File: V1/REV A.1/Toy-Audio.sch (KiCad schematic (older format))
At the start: 18 parts, among them J1 CONN_2, J2 CONN_01X04, J3 CONN_01X10, Q1 Si2302DS, U1 XC6206P332MR, U2 STM32F030F4P6, U3 W25Q32FVSIG

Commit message: Added Standby mode to software V1. Modified hardware to support Standby (add pull up/down resistors) todo hardware V3
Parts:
- removed SP1: 16Ohm, MvdL:JST-PH-2P-DUAL, symbol SPEAKER
- added R?: 1k5, MvdL:R0603, symbol RR
- added SP1: CONN_01X02, symbol CONN_01X02
- C4: value 10u -> 1u
- C8: value d.n.p -> 22n
- Q1: value Si2302DS -> DNP
- R3: value 0R -> DNP
- U3: value W25Q32FVSIG -> W25Q128FVSIG
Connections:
- net labels added: ~CS-FL
- net labels removed: nCS
- wire segments 84 -> 85
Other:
- note added: "10n"
- note added: "1k5"
- note added: "LPF with 4KHz cutoff to filter \nout the PWM base frequency"
- note added: "Modified circuit for audio output (connect audio amp to audio out)"
- note added: "PA0 = WKUP1"
- note added: "audio out"
- note added: "connect to ground"
- note added: "replace Q1 by a 1k resistor\nbetween G and D"
- note removed: "12k"
- note removed: "3V"
- note removed: "Do not place U1 when using 3V battery power\nbypass pin 2 and 3"
- note removed: "Optional HPF with 4KHz cutoff to filter \nout the PWM base frequency"
- note removed: "d.n.p. = do not place"
- moved on the sheet: C10, C8, R3

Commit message: Improved Wake-up pin stability WKUP1. modiefied schematic files. Software V1 is compatible with hardware V2
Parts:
- C8: value 22n -> 47n
- R?: value 1k5 -> d.n.p
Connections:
- net UART1_EN renamed ~Mute
- net USART1_CTS renamed WKUP1
- net ~CS-FL renamed ~CS0
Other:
- note added: "100k"
- note added: "10k"
- note added: "910R"
- note added: "replace Q1 by a 910 Ohm resistor\nbetween G and D"
- note removed: "10n"
- note removed: "1k5"
- note removed: "replace Q1 by a 1k resistor\nbetween G and D"
- moved on the sheet: J3
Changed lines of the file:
@@
 Text Notes 1250 3150 0    60   ~ 0
 STLink SWD Interface
-Text Label 6800 2450 0    60   ~ 0
+Text Label 7375 2475 0    60   ~ 0
 SCL1
-Text Label 6800 2350 0    60   ~ 0
+Text Label 7375 2375 0    60   ~ 0
 SDA1
 $Comp
@@
 $EndComp
 Text Label 5450 4300 0    60   ~ 0
-~CS-FL
+~CS0
 Text Notes 1250 4850 0    60   ~ 0
 Battery Power
@@
 	1    0    0    -1
 $EndComp
-Text Label 6800 2150 0    60   ~ 0
+Text Label 7375 2175 0    60   ~ 0
 USART1_TX
-Text Label 6800 2050 0    60   ~ 0
+Text Label 7375 2075 0    60   ~ 0
 USART1_RX
-Text Label 6800 1950 0    60   ~ 0
+Text Label 7375 1975 0    60   ~ 0
 USART1_CK
-Text Label 6800 1750 0    60   ~ 0
-UART1_EN
+Text Label 7375 1775 0    60   ~ 0
+~Mute
 $Comp
 L GND #PWR21
 U 1 1 55E01A86
-P 7500 2550
-F 0 "#PWR21" H 7500 2300 50  0001 C CNN
-F 1 "GND" H 7500 2400 50  0000 C CNN
-F 2 "" H 7500 2550 60  0000 C CNN
-F 3 "" H 7500 2550 60  0000 C CNN
-	1    7500 2550
+P 8075 2575
+F 0 "#PWR21" H 8075 2325 50  0001 C CNN
+F 1 "GND" H 8075 2425 50  0000 C CNN
+F 2 "" H 8075 2575 60  0000 C CNN
+F 3 "" H 8075 2575 60  0000 C CNN
+	1    8075 2575
 	1    0    0    -1
 $EndComp
@@
 L VDD #PWR20
 U 1 1 55E01CC1
-P 7400 1550
-F 0 "#PWR20" H 7400 1400 50  0001 C CNN
-F 1 "VDD" H 7400 1700 50  0000 C CNN
-F 2 "" H 7400 1550 60  0000 C CNN
-F 3 "" H 7400 1550 60  0000 C CNN
-	1    7400 1550
-	1    0    0    -1
-$EndComp
-Text Notes 7000 2950 0    60   ~ 0
+P 7975 1575
+F 0 "#PWR20" H 7975 1425 50  0001 C CNN
+F 1 "VDD" H 7975 1725 50  0000 C CNN
+F 2 "" H 7975 1575 60  0000 C CNN
+F 3 "" H 7975 1575 60  0000 C CNN
+	1    7975 1575
+	1    0    0    -1
+$EndComp
+Text Notes 7575 2975 0    60   ~ 0
 nRF24L01 interface\n+I2C
 $Comp
@@
 P 9200 3450
 F 0 "C8" H 9200 3550 40  0000 L CNN
-F 1 "22n" H 9206 3365 40  0000 L CNN
+F 1 "47n" H 9206 3365 40  0000 L CNN
 F 2 "MvdL:C0603" H 9238 3300 30  0001 C CNN
 F 3 "~" H 9200 3450 60  0000 C CNN
@@
 PWM
 Text Label 3300 1700 0    60   ~ 0
-~CS-FL
+~CS0
 Text Label 6050 2500 2    60   ~ 0
 SCK1
@@
 USART1_CK
 Text Label 3300 2100 0    60   ~ 0
-USART1_CTS
-Text Label 6800 1850 0    60   ~ 0
-USART1_CTS
+WKUP1
+Text Label 7375 1875 0    60   ~ 0
+WKUP1
 Text Label 3300 2200 0    60   ~ 0
 USART1_RTS
-Text Label 6800 2250 0    60   ~ 0
+Text Label 7375 2275 0    60   ~ 0
 USART1_RTS
 Text Label 6050 1600 2    60   ~ 0
@@
 SCL1
 Text Label 3300 1800 0    60   ~ 0
-UART1_EN
+~Mute
 $Comp
 L VCC #PWR2
@@
 L CONN_01X10 J3
 U 1 1 55EE328F
-P 7800 2000
-F 0 "J3" H 7800 2550 50  0000 C CNN
-F 1 "CONN_01X10" V 7900 2000 50  0000 C CNN
-F 2 "MvdL:HDR_5x2" H 7800 2000 60  0001 C CNN
-F 3 "" H 7800 2000 60  0000 C CNN
-	1    7800 2000
+P 8375 2025
+F 0 "J3" H 8375 2575 50  0000 C CNN
+F 1 "CONN_01X10" V 8475 2025 50  0000 C CNN
+F 2 "MvdL:HDR_5x2" H 8375 2025 60  0001 C CNN
+F 3 "" H 8375 2025 60  0000 C CNN
+	1    8375 2025
 	1    0    0    -1
 $EndComp
@@
 P 8950 3450
 F 0 "R?" V 9030 3450 50  0000 C CNN
-F 1 "1k5" V 8875 3450 50  0000 C CNN
+F 1 "d.n.p" V 8875 3450 50  0000 C CNN
 F 2 "MvdL:R0603" H 8950 3450 60  0001 C CNN
 F 3 "" H 8950 3450 60  0000 C CNN
@@
 	5050 4750 5050 4800
 Wire Wire Line
-	7500 2550 7500 1550
-Wire Wire Line
-	7500 1550 7600 1550
-Wire Wire Line
-	7600 1650 7400 1650
-Wire Wire Line
-	7400 1650 7400 1550
-Wire Wire Line
-	6800 1750 7600 1750
-Wire Wire Line
-	6800 1850 7600 1850
-Wire Wire Line
-	6800 1950 7600 1950
-Wire Wire Line
-	6800 2050 7600 2050
-Wire Wire Line
-	6800 2150 7600 2150
-Wire Wire Line
-	6800 2250 7600 2250
+	8075 2575 8075 1575
+Wire Wire Line
+	8075 1575 8175 1575
+Wire Wire Line
+	8175 1675 7975 1675
+Wire Wire Line
+	7975 1675 7975 1575
+Wire Wire Line
+	7375 1775 8175 1775
+Wire Wire Line
+	7375 1875 8175 1875
+Wire Wire Line
+	7375 1975 8175 1975
+Wire Wire Line
+	7375 2075 8175 2075
+Wire Wire Line
+	7375 2175 8175 2175
+Wire Wire Line
+	7375 2275 8175 2275
 Wire Wire Line
 	9200 4250 9200 4350
@@
 	6200 2000 5700 2000
 Wire Wire Line
-	6800 2350 7600 2350
-Wire Wire Line
-	7600 2450 6800 2450
+	7375 2375 8175 2375
+Wire Wire Line
+	8175 2475 7375 2475
 Wire Wire Line
 	2450 1800 2450 1850
@@
 	8950 3250 8950 3200
 Connection ~ 9200 3200
-Text Notes 7700 4450 0    60   ~ 0
-replace Q1 by a 1k resistor\nbetween G and D
+Text Notes 7525 4450 0    60   ~ 0
+replace Q1 by a 910 Ohm resistor\nbetween G and D
 Wire Notes Line
 	9050 2700 9400 3100
@@
 Wire Notes Line
 	9100 3950 9300 4200
-Text Notes 8850 3900 0    60   ~ 0
-1k5
+Text Notes 8800 3900 0    60   ~ 0
+910R
 Wire Notes Line
 	10400 3350 10800 3750
@@
 Text Notes 9550 3750 0    60   ~ 0
 audio out
-Wire Notes Line
-	9350 3950 9550 3950
-Wire Notes Line
-	9350 4000 9550 4000
-Wire Notes Line
-	9450 3950 9450 3850
-Wire Notes Line
-	9450 3850 9200 3850
-Wire Notes Line
-	9450 4000 9450 4250
-Wire Notes Line
-	9450 4250 9200 4250
-Text Notes 9550 4100 0    60   ~ 0
-10n
 Entry Bus Bus
 	4600 7250 4700 7350
@@
 Text Notes 7800 4750 0    60   ~ 0
 Modified circuit for audio output (connect audio amp to audio out)
+Wire Notes Line
+	7375 1875 7175 1875
+Wire Notes Line
+	7175 1875 7175 1925
+Wire Notes Line
+	7175 1925 7125 1950
+Wire Notes Line
+	7125 1950 7225 1975
+Wire Notes Line
+	7225 1975 7125 2000
+Wire Notes Line
+	7125 2000 7225 2025
+Wire Notes Line
+	7225 2025 7125 2050
+Wire Notes Line
+	7125 2050 7225 2075
+Wire Notes Line
+	7225 2075 7175 2100
+Wire Notes Line
+	7175 2100 7175 2550
+Wire Notes Line
+	7125 2550 7225 2550
+Wire Notes Line
+	7125 2550 7175 2600
+Wire Notes Line
+	7175 2600 7225 2550
+Wire Notes Line
+	7375 1775 6975 1775
+Wire Notes Line
+	6975 1775 6975 1900
+Wire Notes Line
+	6975 1900 6925 1925
+Wire Notes Line
+	6925 1925 7025 1950
+Wire Notes Line
+	7025 1950 6925 1975
+Wire Notes Line
+	6925 1975 7025 2000
+Wire Notes Line
+	7025 2000 6925 2025
+Wire Notes Line
+	6925 2025 7025 2050
+Wire Notes Line
+	7025 2050 6925 2075
+Wire Notes Line
+	6925 2075 6975 2100
+Wire Notes Line
+	6975 2100 6975 2550
+Wire Notes Line
+	6925 2550 7025 2550
+Wire Notes Line
+	6925 2550 6975 2600
+Wire Notes Line
+	6975 2600 7025 2550
+Text Notes 6700 1975 0    60   ~ 0
+100k
+Text Notes 7200 2175 0    60   ~ 0
+10k
 $EndSCHEMATC

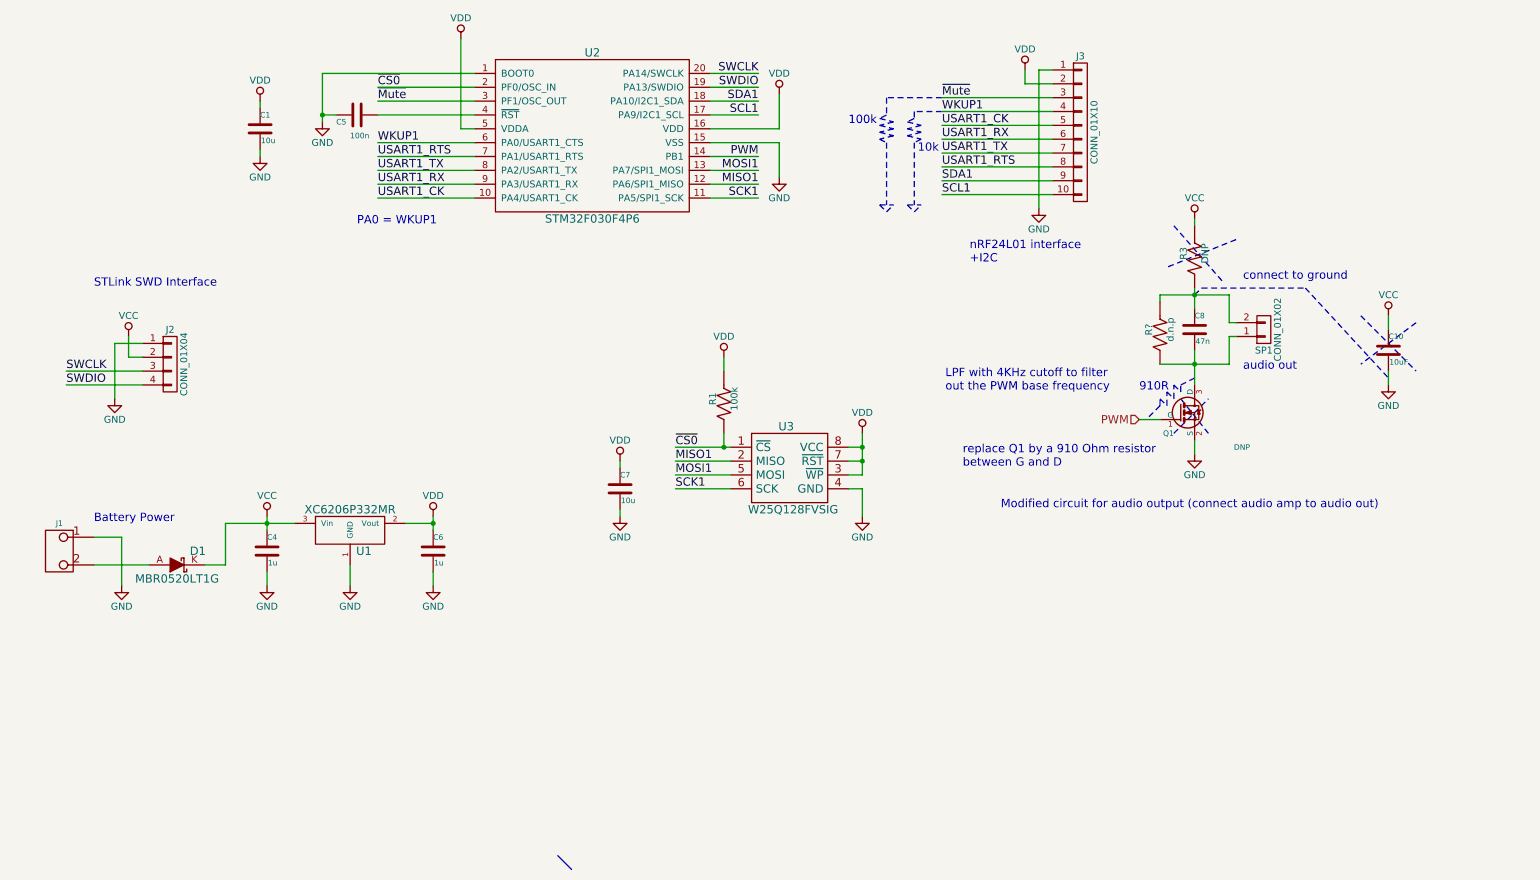
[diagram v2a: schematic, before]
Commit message: Modified/added documentation HW V1. changed SPI flash write function to wait for data transmision complete flag.
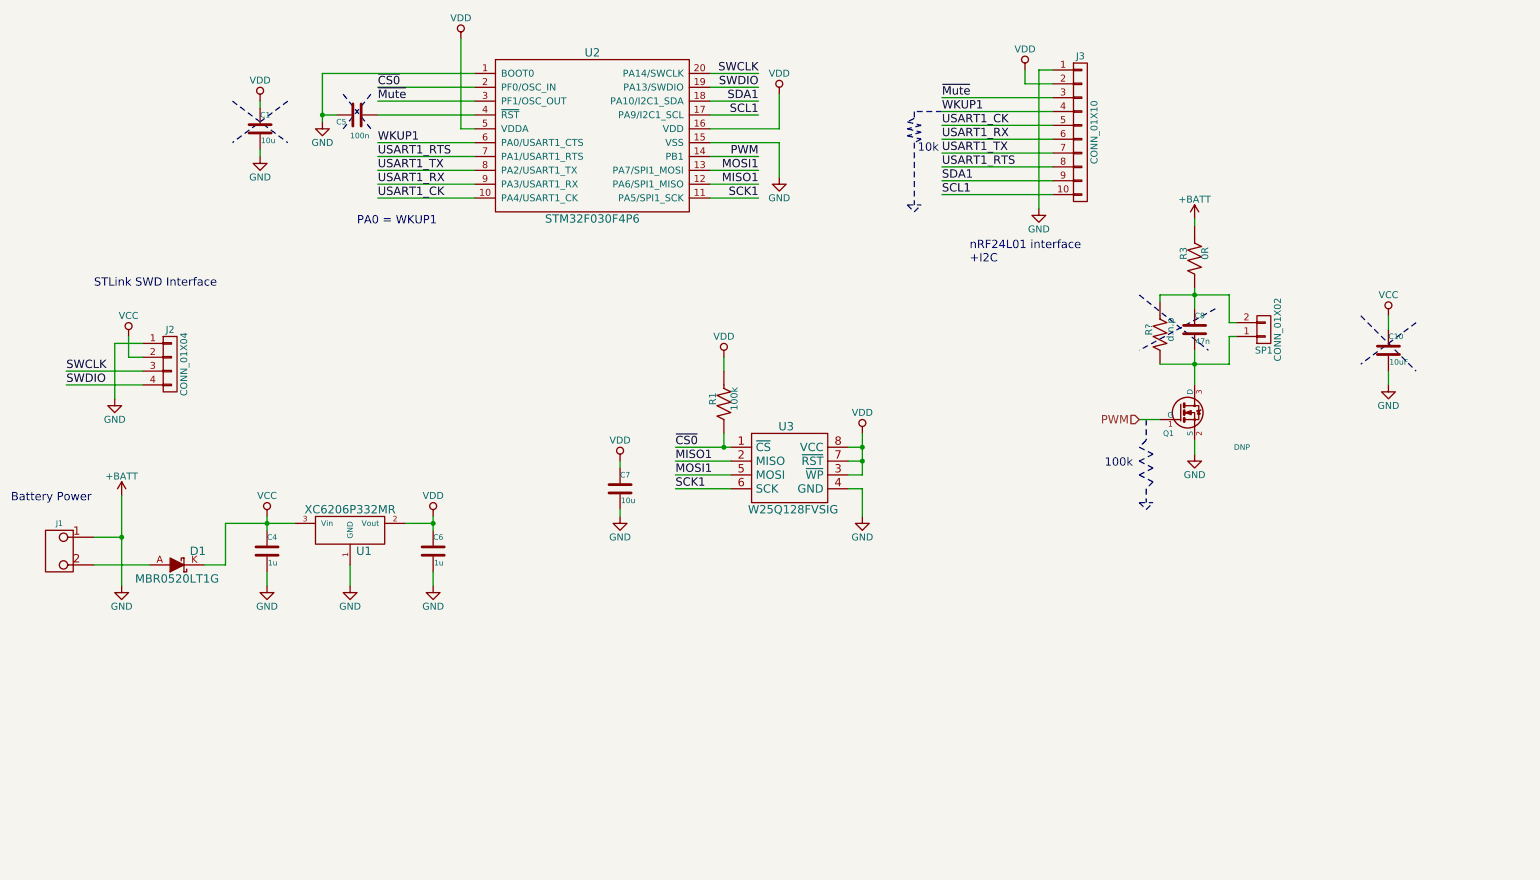
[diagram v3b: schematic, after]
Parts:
- R3: value DNP -> 0R
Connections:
- net VCC: no longer R3.2
- net GND renamed +BATT
- net +BATT: now also R3.2
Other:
- note removed: "910R"
- note removed: "LPF with 4KHz cutoff to filter \nout the PWM base frequency"
- note removed: "Modified circuit for audio output (connect audio amp to audio out)"
- note removed: "audio out"
- note removed: "connect to ground"
- note removed: "replace Q1 by a 910 Ohm resistor\nbetween G and D"
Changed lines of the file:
@@
 Sheet 1 1
 Title "Toy Audio V1"
-Date "5 aug 2015"
+Date "2016-02-07"
 Rev "A.1"
 Comp "Maurits van de Lande (maurits@vandelande.com)"
@@
 Text Label 5450 4300 0    60   ~ 0
 ~CS0
-Text Notes 1250 4850 0    60   ~ 0
+Text Notes 650  4700 0    60   ~ 0
 Battery Power
 Text Label 1050 3750 0    60   ~ 0
@@
 P 9200 2900
 F 0 "R3" V 9280 2900 50  0000 C CNN
-F 1 "DNP" V 9125 2900 50  0000 C CNN
+F 1 "0R" V 9125 2900 50  0000 C CNN
 F 2 "MvdL:R0603" H 9200 2900 60  0001 C CNN
 F 3 "" H 9200 2900 60  0000 C CNN
@@
 $EndComp
 $Comp
-L VCC #PWR22
-U 1 1 55EE2A6B
-P 9200 2650
-F 0 "#PWR22" H 9200 2500 50  0001 C CNN
-F 1 "VCC" H 9200 2800 50  0000 C CNN
-F 2 "" H 9200 2650 60  0000 C CNN
-F 3 "" H 9200 2650 60  0000 C CNN
-	1    9200 2650
-	1    0    0    -1
-$EndComp
-$Comp
 L CONN_01X10 J3
 U 1 1 55EE328F
@@
 	1    0    0    -1
 $EndComp
-Text Notes 7400 3900 0    60   ~ 0
-LPF with 4KHz cutoff to filter \nout the PWM base frequency
 $Comp
 L CONN_01X02 SP1
@@
 	2500 5300 2500 5200
 Wire Wire Line
-	1450 5300 1450 4950
+	1450 4650 1450 5300
 Wire Wire Line
 	1450 4950 1250 4950
@@
 	8950 3250 8950 3200
 Connection ~ 9200 3200
-Text Notes 7525 4450 0    60   ~ 0
-replace Q1 by a 910 Ohm resistor\nbetween G and D
-Wire Notes Line
-	9050 2700 9400 3100
-Wire Notes Line
-	9500 2800 9000 3000
-Wire Notes Line
-	8950 4000 8950 3950
-Wire Notes Line
-	8950 3950 9000 4000
-Wire Notes Line
-	9000 4000 9000 3900
-Wire Notes Line
-	9000 3900 9050 3950
-Wire Notes Line
-	9050 3950 9050 3850
-Wire Notes Line
-	9050 3850 9100 3900
-Wire Notes Line
-	9100 3900 9100 3850
-Wire Notes Line
-	9100 3850 9200 3800
-Wire Notes Line
-	8950 4000 8850 4100
-Wire Notes Line
-	9050 4200 9300 3950
-Wire Notes Line
-	9100 3950 9300 4200
-Text Notes 8800 3900 0    60   ~ 0
-910R
 Wire Notes Line
 	10400 3350 10800 3750
 Wire Notes Line
 	10800 3400 10400 3700
-Wire Notes Line
-	10000 3150 10600 3800
-Wire Wire Line
-	8950 3200 9450 3200
-Wire Notes Line
-	9200 3200 9250 3150
-Wire Notes Line
-	9250 3150 10000 3150
-Text Notes 9550 3100 0    60   ~ 0
-connect to ground
-Text Notes 9550 3750 0    60   ~ 0
-audio out
-Entry Bus Bus
-	4600 7250 4700 7350
 Text Notes 3150 2700 0    60   ~ 0
 PA0 = WKUP1
-Text Notes 7800 4750 0    60   ~ 0
-Modified circuit for audio output (connect audio amp to audio out)
 Wire Notes Line
 	7375 1875 7175 1875
@@
 Wire Notes Line
 	7175 2600 7225 2550
-Wire Notes Line
-	7375 1775 6975 1775
-Wire Notes Line
-	6975 1775 6975 1900
-Wire Notes Line
-	6975 1900 6925 1925
-Wire Notes Line
-	6925 1925 7025 1950
-Wire Notes Line
-	7025 1950 6925 1975
-Wire Notes Line
-	6925 1975 7025 2000
-Wire Notes Line
-	7025 2000 6925 2025
-Wire Notes Line
-	6925 2025 7025 2050
-Wire Notes Line
-	7025 2050 6925 2075
-Wire Notes Line
-	6925 2075 6975 2100
-Wire Notes Line
-	6975 2100 6975 2550
-Wire Notes Line
-	6925 2550 7025 2550
-Wire Notes Line
-	6925 2550 6975 2600
-Wire Notes Line
-	6975 2600 7025 2550
-Text Notes 6700 1975 0    60   ~ 0
-100k
 Text Notes 7200 2175 0    60   ~ 0
 10k
+Wire Wire Line
+	8950 3200 9450 3200
+Wire Notes Line
+	8800 3200 9300 3600
+Wire Notes Line
+	9350 3300 8800 3600
+Wire Notes Line
+	8850 4100 8850 4250
+Wire Notes Line
+	8850 4250 8800 4300
+Wire Notes Line
+	8800 4300 8900 4350
+Wire Notes Line
+	8900 4350 8800 4400
+Wire Notes Line
+	8800 4400 8900 4450
+Wire Notes Line
+	8900 4450 8800 4500
+Wire Notes Line
+	8800 4500 8900 4550
+Wire Notes Line
+	8900 4550 8850 4600
+Wire Notes Line
+	8850 4600 8850 4700
+Wire Notes Line
+	8800 4700 8900 4700
+Wire Notes Line
+	8800 4700 8850 4750
+Wire Notes Line
+	8850 4750 8900 4700
+Text Notes 8550 4450 0    60   ~ 0
+100k
+$Comp
+L +BATT #PWR?
+U 1 1 56B7E010
+P 9200 2650
+F 0 "#PWR?" H 9200 2500 50  0001 C CNN
+F 1 "+BATT" H 9200 2790 50  0000 C CNN
+F 2 "" H 9200 2650 50  0000 C CNN
+F 3 "" H 9200 2650 50  0000 C CNN
+	1    9200 2650
+	1    0    0    -1
+$EndComp
+$Comp
+L +BATT #PWR?
+U 1 1 56B7E196
+P 1450 4650
+F 0 "#PWR?" H 1450 4500 50  0001 C CNN
+F 1 "+BATT" H 1450 4790 50  0000 C CNN
+F 2 "" H 1450 4650 50  0000 C CNN
+F 3 "" H 1450 4650 50  0000 C CNN
+	1    1450 4650
+	1    0    0    -1
+$EndComp
+Connection ~ 1450 4950
+Wire Notes Line
+	3050 1750 3250 2000
+Wire Notes Line
+	3250 1750 3050 2000
+Wire Notes Line
+	2250 1800 2650 2100
+Wire Notes Line
+	2650 1800 2250 2100
 $EndSCHEMATC
